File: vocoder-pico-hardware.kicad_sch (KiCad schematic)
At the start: 50 parts, among them J1 Conn_02x05_Odd_Even, J2 AudioJack2_SwitchT, J3 AudioJack2_SwitchT, SW1 SW_Push, SW2 SW_Push, U1 TL072, U2 LM7805_TO220, U3 PCM5100A, U8 MCP6002-xP

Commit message: replace certain capacitors with 0805
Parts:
- C12, C17, C9: footprint Capacitor_THT:CP_Radial_D5.0mm_P2.00mm -> Capacitor_SMD:C_0805_2012Metric
- C14, C15, C19, C20, C22, C23, C26, C28: footprint Capacitor_THT:C_Disc_D5.0mm_W2.5mm_P5.00mm -> Capacitor_SMD:C_0805_2012Metric
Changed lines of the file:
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@@
 			)
 		)
-		(property "Footprint" "Capacitor_THT:C_Disc_D5.0mm_W2.5mm_P5.00mm"
+		(property "Footprint" "Capacitor_SMD:C_0805_2012Metric"
 			(at 262.5852 66.04 0)
 			(effects
@@
 			)
 		)
-		(property "Footprint" "Capacitor_THT:CP_Radial_D5.0mm_P2.00mm"
+		(property "Footprint" "Capacitor_SMD:C_0805_2012Metric"
 			(at 248.6152 40.64 0)
 			(effects
@@
 			)
 		)
-		(property "Footprint" "Capacitor_THT:C_Disc_D5.0mm_W2.5mm_P5.00mm"
+		(property "Footprint" "Capacitor_SMD:C_0805_2012Metric"
 			(at 251.1552 71.12 0)
 			(effects
@@
 			)
 		)
-		(property "Footprint" "Capacitor_THT:CP_Radial_D5.0mm_P2.00mm"
+		(property "Footprint" "Capacitor_SMD:C_0805_2012Metric"
 			(at 210.5152 52.07 0)
 			(effects
@@
 			)
 		)
-		(property "Footprint" "Capacitor_THT:C_Disc_D5.0mm_W2.5mm_P5.00mm"
+		(property "Footprint" "Capacitor_SMD:C_0805_2012Metric"
 			(at 251.1552 86.36 0)
 			(effects
@@
 			)
 		)
-		(property "Footprint" "Capacitor_THT:C_Disc_D5.0mm_W2.5mm_P5.00mm"
+		(property "Footprint" "Capacitor_SMD:C_0805_2012Metric"
 			(at 272.7452 83.82 0)
 			(effects
@@
 			)
 		)
-		(property "Footprint" "Capacitor_THT:C_Disc_D5.0mm_W2.5mm_P5.00mm"
+		(property "Footprint" "Capacitor_SMD:C_0805_2012Metric"
 			(at 225.7552 35.56 0)
 			(effects
@@
 			)
 		)
-		(property "Footprint" "Capacitor_THT:C_Disc_D5.0mm_W2.5mm_P5.00mm"
+		(property "Footprint" "Capacitor_SMD:C_0805_2012Metric"
 			(at 256.2352 39.37 0)
 			(effects
@@
 			)
 		)
-		(property "Footprint" "Capacitor_THT:C_Disc_D5.0mm_W2.5mm_P5.00mm"
+		(property "Footprint" "Capacitor_SMD:C_0805_2012Metric"
 			(at 218.1352 50.8 0)
 			(effects
@@
 			)
 		)
-		(property "Footprint" "Capacitor_THT:C_Disc_D5.0mm_W2.5mm_P5.00mm"
+		(property "Footprint" "Capacitor_SMD:C_0805_2012Metric"
 			(at 270.2052 63.5 0)
 			(effects
@@
 			)
 		)
-		(property "Footprint" "Capacitor_THT:CP_Radial_D5.0mm_P2.00mm"
+		(property "Footprint" "Capacitor_SMD:C_0805_2012Metric"
 			(at 218.1352 36.83 0)
 			(effects

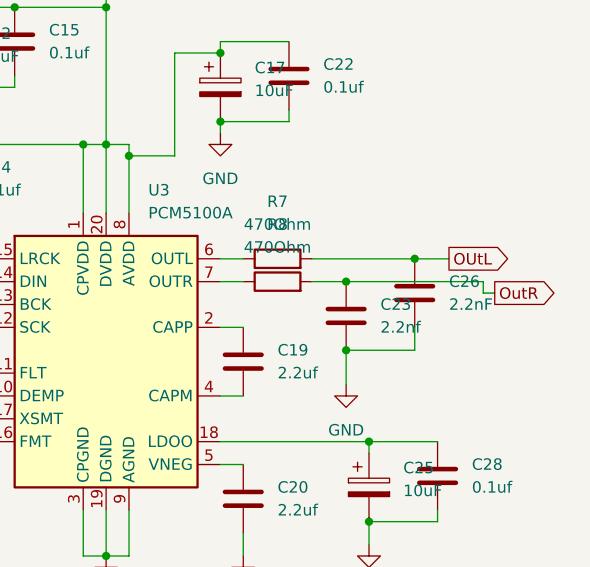
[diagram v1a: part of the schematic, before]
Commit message: reposition C22
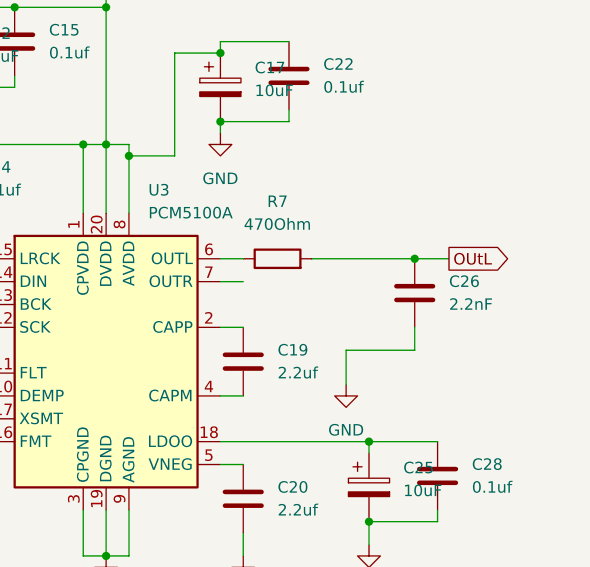
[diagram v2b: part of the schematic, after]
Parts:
- removed C23: 2.2nf, Capacitor_SMD:C_0805_2012Metric, symbol Device:C
- removed R8: 470Ohm, Resistor_SMD:R_0805_2012Metric, symbol Device:R
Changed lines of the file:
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@@
 	)
 	(junction
-		(at 261.62 66.04)
-		(diameter 0)
-		(color 0 0 0 0)
-	)
-	(junction
 		(at 54.61 158.75)
 		(diameter 0)
@@
 	)
 	(junction
-		(at 261.62 58.42)
-		(diameter 0)
-		(color 0 0 0 0)
-	)
-	(junction
 		(at 87.63 170.18)
 		(diameter 0)
@@
 	(wire
 		(pts
-			(xy 261.62 58.42) (xy 276.86 58.42)
-		)
-		(stroke
-			(width 0)
-			(type default)
-		)
-	)
-	(wire
-		(pts
 			(xy 142.24 72.39) (xy 154.94 72.39)
 		)
@@
 	(wire
 		(pts
-			(xy 276.86 58.42) (xy 276.86 59.69)
-		)
-		(stroke
-			(width 0)
-			(type default)
-		)
-	)
-	(wire
-		(pts
 			(xy 78.74 128.27) (xy 78.74 135.89)
 		)
@@
 	(wire
 		(pts
-			(xy 257.81 58.42) (xy 261.62 58.42)
-		)
-		(stroke
-			(width 0)
-			(type default)
-		)
-	)
-	(wire
-		(pts
 			(xy 142.24 77.47) (xy 154.94 77.47)
 		)
@@
 	(wire
 		(pts
-			(xy 276.86 59.69) (xy 278.13 59.69)
-		)
-		(stroke
-			(width 0)
-			(type default)
-		)
-	)
-	(wire
-		(pts
 			(xy 220.98 107.95) (xy 220.98 115.57)
 		)
@@
 		)
 	)
-	(global_label "OutR"
-		(shape output)
-		(at 278.13 59.69 0)
-		(fields_autoplaced yes)
-		(effects
-			(font
-				(size 1.27 1.27)
-			)
-			(justify left)
-		)
-		(property "Intersheetrefs" "${INTERSHEET_REFS}"
-			(at 285.5904 59.69 0)
-			(effects
-				(font
-					(size 1.27 1.27)
-				)
-				(justify left)
-				(hide yes)
-			)
-		)
-	)
 	(symbol
 		(lib_id "Diode:1N5817")
@@
 	)
 	(symbol
-		(lib_id "Device:C")
-		(at 261.62 62.23 0)
-		(unit 1)
-		(exclude_from_sim no)
-		(in_bom yes)
-		(on_board yes)
-		(dnp no)
-		(fields_autoplaced yes)
-		(property "Reference" "C23"
-			(at 265.43 60.9599 0)
-			(effects
-				(font
-					(size 1.27 1.27)
-				)
-				(justify left)
-			)
-		)
-		(property "Value" "2.2nf"
-			(at 265.43 63.4999 0)
-			(effects
-				(font
-					(size 1.27 1.27)
-				)
-				(justify left)
-			)
-		)
-		(property "Footprint" "Capacitor_SMD:C_0805_2012Metric"
-			(at 262.5852 66.04 0)
-			(effects
-				(font
-					(size 1.27 1.27)
-				)
-				(hide yes)
-			)
-		)
-		(property "Datasheet" "~"
-			(at 261.62 62.23 0)
-			(effects
-				(font
-					(size 1.27 1.27)
-				)
-				(hide yes)
-			)
-		)
-		(property "Description" "Unpolarized capacitor"
-			(at 261.62 62.23 0)
-			(effects
-				(font
-					(size 1.27 1.27)
-				)
-				(hide yes)
-			)
-		)
-		(pin "2"
-		)
-		(pin "1"
-		)
-		(instances
-			(project ""
-				(path "/68f2073a-7618-4fa5-a11d-b71bb4f75794"
-					(reference "C23")
-					(unit 1)
-				)
-			)
-		)
-	)
-	(symbol
 		(lib_id "Device:R")
 		(at 83.82 135.89 90)
@@
 					(unit 1)
 				)
-			)
-		)
-	)
-	(symbol
-		(lib_id "Device:R")
-		(at 254 58.42 90)
-		(unit 1)
-		(exclude_from_sim no)
-		(in_bom yes)
-		(on_board yes)
-		(dnp no)
-		(fields_autoplaced yes)
-		(property "Reference" "R8"
-			(at 254 52.07 90)
-			(effects
-				(font
-					(size 1.27 1.27)
-				)
-			)
-		)
-		(property "Value" "470Ohm"
-			(at 254 54.61 90)
-			(effects
-				(font
-					(size 1.27 1.27)
-				)
-			)
-		)
-		(property "Footprint" "Resistor_SMD:R_0805_2012Metric"
-			(at 254 60.198 90)
-			(effects
-				(font
-					(size 1.27 1.27)
-				)
-				(hide yes)
-			)
-		)
-		(property "Datasheet" "~"
-			(at 254 58.42 0)
-			(effects
-				(font
-					(size 1.27 1.27)
-				)
-				(hide yes)
-			)
-		)
-		(property "Description" "Resistor"
-			(at 254 58.42 0)
-			(effects
-				(font
-					(size 1.27 1.27)
-				)
-				(hide yes)
-			)
-		)
-		(pin "2"
-		)
-		(pin "1"
-		)
-		(instances
-			(project "vocoder-pico-hardware"
-				(path "/68f2073a-7618-4fa5-a11d-b71bb4f75794"
-					(reference "R8")
-					(unit 1)
-				)

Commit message: make polarized capacitators consistent
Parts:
- C3, C4, C6: footprint Capacitor_THT:CP_Radial_D8.0mm_P3.80mm -> Capacitor_THT:CP_Radial_D5.0mm_P2.00mm
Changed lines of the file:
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@@
 			)
 		)
-		(property "Footprint" "Capacitor_THT:CP_Radial_D8.0mm_P3.80mm"
+		(property "Footprint" "Capacitor_THT:CP_Radial_D5.0mm_P2.00mm"
 			(at 143.2052 182.88 0)
 			(effects
@@
 			)
 		)
-		(property "Footprint" "Capacitor_THT:CP_Radial_D8.0mm_P3.80mm"
+		(property "Footprint" "Capacitor_THT:CP_Radial_D5.0mm_P2.00mm"
 			(at 89.8652 187.96 0)
 			(effects
@@
 			)
 		)
-		(property "Footprint" "Capacitor_THT:CP_Radial_D8.0mm_P3.80mm"
+		(property "Footprint" "Capacitor_THT:CP_Radial_D5.0mm_P2.00mm"
 			(at 119.0752 182.88 0)
 			(effects

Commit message: rename u1 => u8, u8 => u1
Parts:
- renumbered U8 to U1, U1 to U8
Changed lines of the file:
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@@
 		(on_board yes)
 		(dnp no)
-		(property "Reference" "U1"
+		(property "Reference" "U8"
 			(at 88.9 184.1501 0)
 			(effects
@@
 			(project ""
 				(path "/68f2073a-7618-4fa5-a11d-b71bb4f75794"
-					(reference "U1")
+					(reference "U8")
 					(unit 3)
 				)
@@
 		(on_board yes)
 		(dnp no)
-		(property "Reference" "U8"
+		(property "Reference" "U1"
 			(at 66.04 158.75 0)
 			(effects
@@
 			(project ""
 				(path "/68f2073a-7618-4fa5-a11d-b71bb4f75794"
-					(reference "U8")
+					(reference "U1")
 					(unit 1)
 				)
@@
 		(on_board yes)
 		(dnp no)
-		(property "Reference" "U8"
+		(property "Reference" "U1"
 			(at 115.57 158.75 0)
 			(effects
@@
 			(project "vocoder-pico-hardware"
 				(path "/68f2073a-7618-4fa5-a11d-b71bb4f75794"
-					(reference "U8")
+					(reference "U1")
 					(unit 2)
 				)
@@
 		(dnp no)
 		(fields_autoplaced yes)
-		(property "Reference" "U1"
+		(property "Reference" "U8"
 			(at 195.58 97.79 0)
 			(effects
@@
 			(project ""
 				(path "/68f2073a-7618-4fa5-a11d-b71bb4f75794"
-					(reference "U1")
+					(reference "U8")
 					(unit 1)
 				)
@@
 		(dnp no)
 		(fields_autoplaced yes)
-		(property "Reference" "U1"
+		(property "Reference" "U8"
 			(at 199.39 138.43 0)
 			(effects
@@
 			(project "vocoder-pico-hardware"
 				(path "/68f2073a-7618-4fa5-a11d-b71bb4f75794"
-					(reference "U1")
+					(reference "U8")
 					(unit 2)
 				)
@@
 		(on_board yes)
 		(dnp no)
-		(property "Reference" "U8"
+		(property "Reference" "U1"
 			(at 152.4 142.24 0)
 			(effects
@@
 			(project "vocoder-pico-hardware"
 				(path "/68f2073a-7618-4fa5-a11d-b71bb4f75794"
-					(reference "U8")
+					(reference "U1")
 					(unit 3)
 				)

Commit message: update schematic
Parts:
- C12, C17, C9: symbol Device:C_Polarized -> Device:C
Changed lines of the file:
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@@
 	)
 	(symbol
-		(lib_id "Device:C_Polarized")
+		(lib_id "Device:C")
 		(at 247.65 36.83 0)
 		(unit 1)
@@
 			)
 		)
-		(property "Description" "Polarized capacitor"
+		(property "Description" "Unpolarized capacitor"
 			(at 247.65 36.83 0)
 			(effects
@@
 	)
 	(symbol
-		(lib_id "Device:C_Polarized")
+		(lib_id "Device:C")
 		(at 209.55 48.26 0)
 		(unit 1)
@@
 		(fields_autoplaced yes)
 		(property "Reference" "C9"
-			(at 213.36 46.1009 0)
+			(at 213.36 46.9899 0)
 			(effects
 				(font
@@
 		)
 		(property "Value" "10uF"
-			(at 213.36 48.6409 0)
+			(at 213.36 49.5299 0)
 			(effects
 				(font
@@
 			)
 		)
-		(property "Description" "Polarized capacitor"
+		(property "Description" "Unpolarized capacitor"
 			(at 209.55 48.26 0)
 			(effects
@@
 	)
 	(symbol
-		(lib_id "Device:C_Polarized")
+		(lib_id "Device:C")
 		(at 217.17 33.02 0)
 		(unit 1)
@@
 		(fields_autoplaced yes)
 		(property "Reference" "C12"
-			(at 220.98 30.8609 0)
+			(at 220.98 31.7499 0)
 			(effects
 				(font
@@
 		)
 		(property "Value" "10uF"
-			(at 220.98 33.4009 0)
+			(at 220.98 34.2899 0)
 			(effects
 				(font
@@
 			)
 		)
-		(property "Description" "Polarized capacitor"
+		(property "Description" "Unpolarized capacitor"
 			(at 217.17 33.02 0)
 			(effects

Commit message: remove the pico module from bom
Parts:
- A1: now not fitted
- C5: value 100nF -> 100n
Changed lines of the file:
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@@
 		(in_bom yes)
 		(on_board yes)
-		(dnp no)
+		(dnp yes)
 		(fields_autoplaced yes)
 		(property "Reference" "A1"
@@
 			)
 		)
-		(property "Value" "100nF"
+		(property "Value" "100n"
 			(at 139.7 180.3399 0)
 			(effects

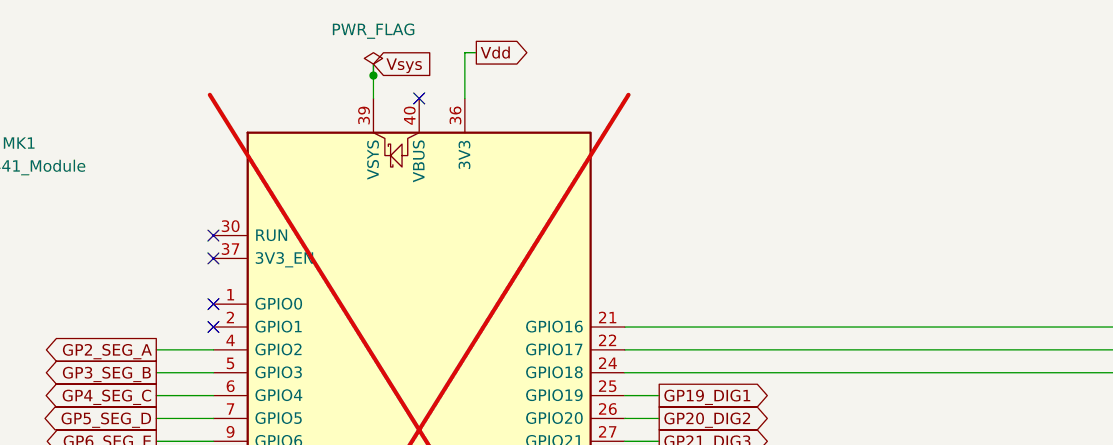
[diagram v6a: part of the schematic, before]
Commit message: add female header for the pico
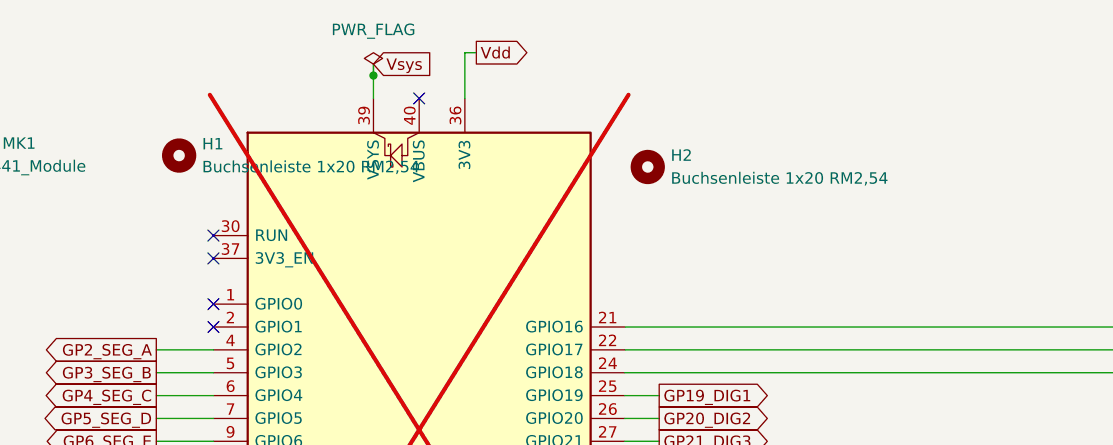
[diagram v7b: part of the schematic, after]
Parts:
- added H1, H2: Buchsenleiste 1x20 RM2,54, symbol Mechanical:MountingHole
- A1: now left out of the parts list
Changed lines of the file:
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@@
 	)
 	(symbol
+		(lib_id "Mechanical:MountingHole")
+		(at 144.78 29.21 0)
+		(unit 1)
+		(exclude_from_sim no)
+		(in_bom yes)
+		(on_board no)
+		(dnp no)
+		(fields_autoplaced yes)
+		(property "Reference" "H2"
+			(at 147.32 27.9399 0)
+			(effects
+				(font
+					(size 1.27 1.27)
+				)
+				(justify left)
+			)
+		)
+		(property "Value" "Buchsenleiste 1x20 RM2,54"
+			(at 147.32 30.4799 0)
+			(effects
+				(font
+					(size 1.27 1.27)
+				)
+				(justify left)
+			)
+		)
+		(property "Footprint" ""
+			(at 144.78 29.21 0)
+			(effects
+				(font
+					(size 1.27 1.27)
+				)
+				(hide yes)
+			)
+		)
+		(property "Datasheet" "~"
+			(at 144.78 29.21 0)
+			(effects
+				(font
+					(size 1.27 1.27)
+				)
+				(hide yes)
+			)
+		)
+		(property "Description" "Mounting Hole without connection"
+			(at 144.78 29.21 0)
+			(effects
+				(font
+					(size 1.27 1.27)
+				)
+				(hide yes)
+			)
+		)
+		(instances
+			(project ""
+				(path "/68f2073a-7618-4fa5-a11d-b71bb4f75794"
+					(reference "H2")
+					(unit 1)
+				)
+			)
+		)
+	)
+	(symbol
 		(lib_id "Amplifier_Operational:TL072")
 		(at 77.47 180.34 0)
@@
 		(unit 1)
 		(exclude_from_sim no)
-		(in_bom yes)
+		(in_bom no)
 		(on_board yes)
 		(dnp yes)
@@
 					(unit 1)
 				)
+			)
+		)
+	)
+	(symbol
+		(lib_id "Mechanical:MountingHole")
+		(at 92.71 27.94 0)
+		(unit 1)
+		(exclude_from_sim no)
+		(in_bom yes)
+		(on_board no)
+		(dnp no)
+		(fields_autoplaced yes)
+		(property "Reference" "H1"
+			(at 95.25 26.6699 0)
+			(effects
+				(font
+					(size 1.27 1.27)
+				)
+				(justify left)
+			)
+		)
+		(property "Value" "Buchsenleiste 1x20 RM2,54"
+			(at 95.25 29.2099 0)
+			(effects
+				(font
+					(size 1.27 1.27)
+				)
+				(justify left)
+			)
+		)
+		(property "Footprint" ""
+			(at 92.71 27.94 0)
+			(effects
+				(font
+					(size 1.27 1.27)
+				)
+				(hide yes)
+			)
+		)
+		(property "Datasheet" "~"
+			(at 92.71 27.94 0)
+			(effects
+				(font
+					(size 1.27 1.27)
+				)
+				(hide yes)
+			)
+		)
+		(property "Description" "Mounting Hole without connection"
+			(at 92.71 27.94 0)
+			(effects
+				(font
+					(size 1.27 1.27)
+				)
+				(hide yes)
+			)
+		)
+		(instances
+			(project ""
+				(path "/68f2073a-7618-4fa5-a11d-b71bb4f75794"
+					(reference "H1")
+					(unit 1)
+				)

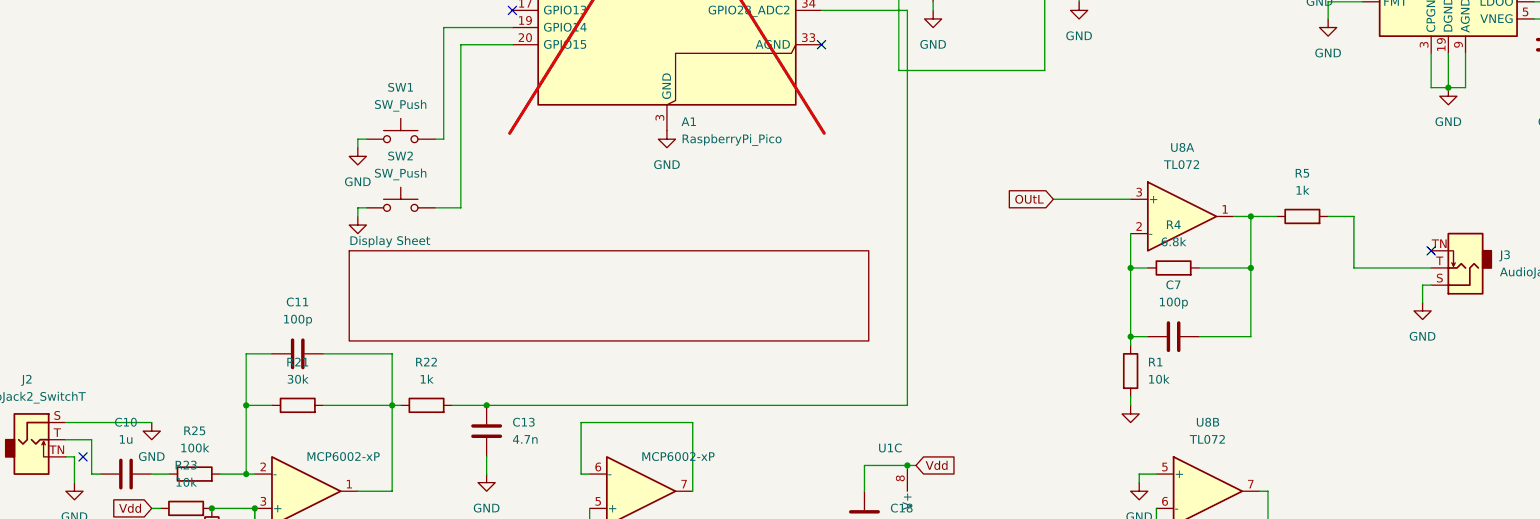
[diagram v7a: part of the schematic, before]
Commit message: add sockets for U1 and U8
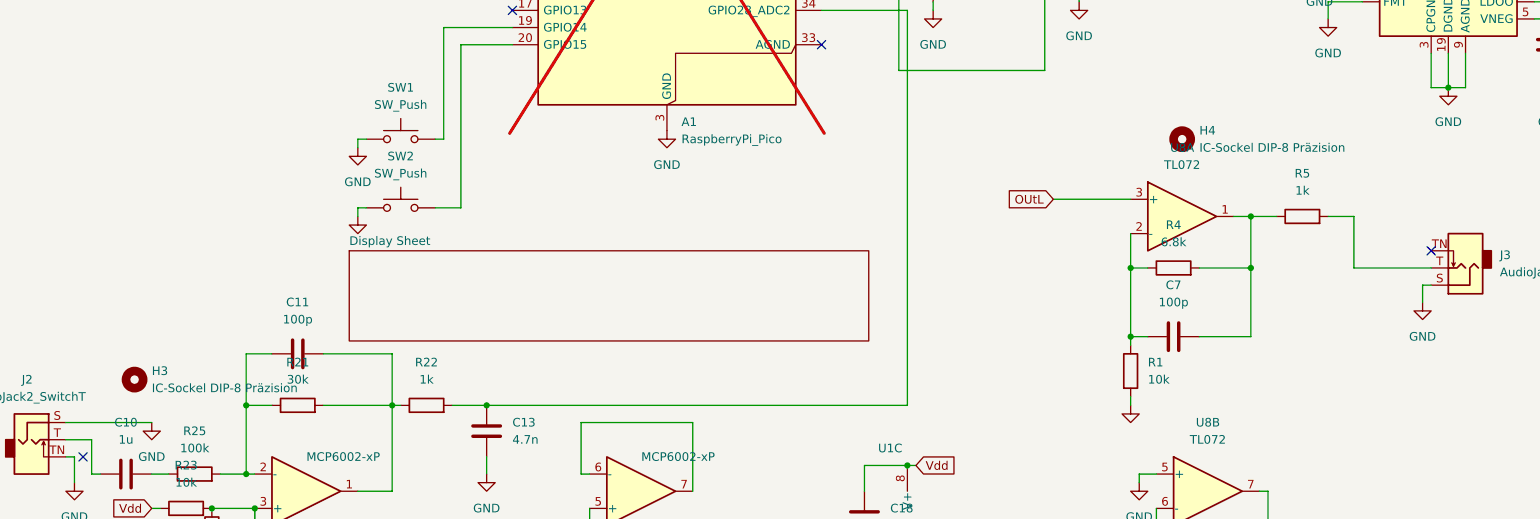
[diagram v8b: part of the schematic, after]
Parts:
- added H3, H4: IC-Sockel DIP-8 Präzision, symbol Mechanical:MountingHole
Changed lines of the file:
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@@
+	)
+	(symbol
+		(lib_id "Mechanical:MountingHole")
+		(at 195.58 96.52 0)
+		(unit 1)
+		(exclude_from_sim no)
+		(in_bom yes)
+		(on_board no)
+		(dnp no)
+		(fields_autoplaced yes)
+		(property "Reference" "H4"
+			(at 198.12 95.2499 0)
+			(effects
+				(font
+					(size 1.27 1.27)
+				)
+				(justify left)
+			)
+		)
+		(property "Value" "IC-Sockel DIP-8 Präzision"
+			(at 198.12 97.7899 0)
+			(effects
+				(font
+					(size 1.27 1.27)
+				)
+				(justify left)
+			)
+		)
+		(property "Footprint" ""
+			(at 195.58 96.52 0)
+			(effects
+				(font
+					(size 1.27 1.27)
+				)
+				(hide yes)
+			)
+		)
+		(property "Datasheet" "~"
+			(at 195.58 96.52 0)
+			(effects
+				(font
+					(size 1.27 1.27)
+				)
+				(hide yes)
+			)
+		)
+		(property "Description" "Mounting Hole without connection"
+			(at 195.58 96.52 0)
+			(effects
+				(font
+					(size 1.27 1.27)
+				)
+				(hide yes)
+			)
+		)
+		(instances
+			(project "vocoder-pico-hardware"
+				(path "/68f2073a-7618-4fa5-a11d-b71bb4f75794"
+					(reference "H4")
+					(unit 1)
+				)
+			)
+		)
 	)
 	(symbol
@@
 					(unit 1)
 				)
+			)
+		)
+	)
+	(symbol
+		(lib_id "Mechanical:MountingHole")
+		(at 40.64 132.08 0)
+		(unit 1)
+		(exclude_from_sim no)
+		(in_bom yes)
+		(on_board no)
+		(dnp no)
+		(fields_autoplaced yes)
+		(property "Reference" "H3"
+			(at 43.18 130.8099 0)
+			(effects
+				(font
+					(size 1.27 1.27)
+				)
+				(justify left)
+			)
+		)
+		(property "Value" "IC-Sockel DIP-8 Präzision"
+			(at 43.18 133.3499 0)
+			(effects
+				(font
+					(size 1.27 1.27)
+				)
+				(justify left)
+			)
+		)
+		(property "Footprint" ""
+			(at 40.64 132.08 0)
+			(effects
+				(font
+					(size 1.27 1.27)
+				)
+				(hide yes)
+			)
+		)
+		(property "Datasheet" "~"
+			(at 40.64 132.08 0)
+			(effects
+				(font
+					(size 1.27 1.27)
+				)
+				(hide yes)
+			)
+		)
+		(property "Description" "Mounting Hole without connection"
+			(at 40.64 132.08 0)
+			(effects
+				(font
+					(size 1.27 1.27)
+				)
+				(hide yes)
+			)
+		)
+		(instances
+			(project ""
+				(path "/68f2073a-7618-4fa5-a11d-b71bb4f75794"
+					(reference "H3")
+					(unit 1)
+				)
